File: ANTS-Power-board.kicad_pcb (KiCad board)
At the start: 2 copper layers, 80 x 80 mm, 35 parts, among them J1 DF11-12DP, J2 DF11-12DP, J3 Phoenix 1751248, J4 Phoenix 1751248, U1 TPS62916RPYR, U2 LP2985-3.3

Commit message: Add production files
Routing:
- net VBAT-: vias 140 -> 145
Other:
- board text added: "JLCJLCJLCJLC"

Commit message: Adjust production files
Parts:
- C1, C2: value 22uF -> 10u
- L1: value 1uH -> XGL5030-102MEC

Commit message: Add decoratives
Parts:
- added G***: LOGO, LOGO, F.Cu at (167.5, 108.5)
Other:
- board text added: "+5V/+3.3V LOW-NOISE POWER SUPPLIES"
- board text added: "Designed by Tri Do & Garrett Davis"

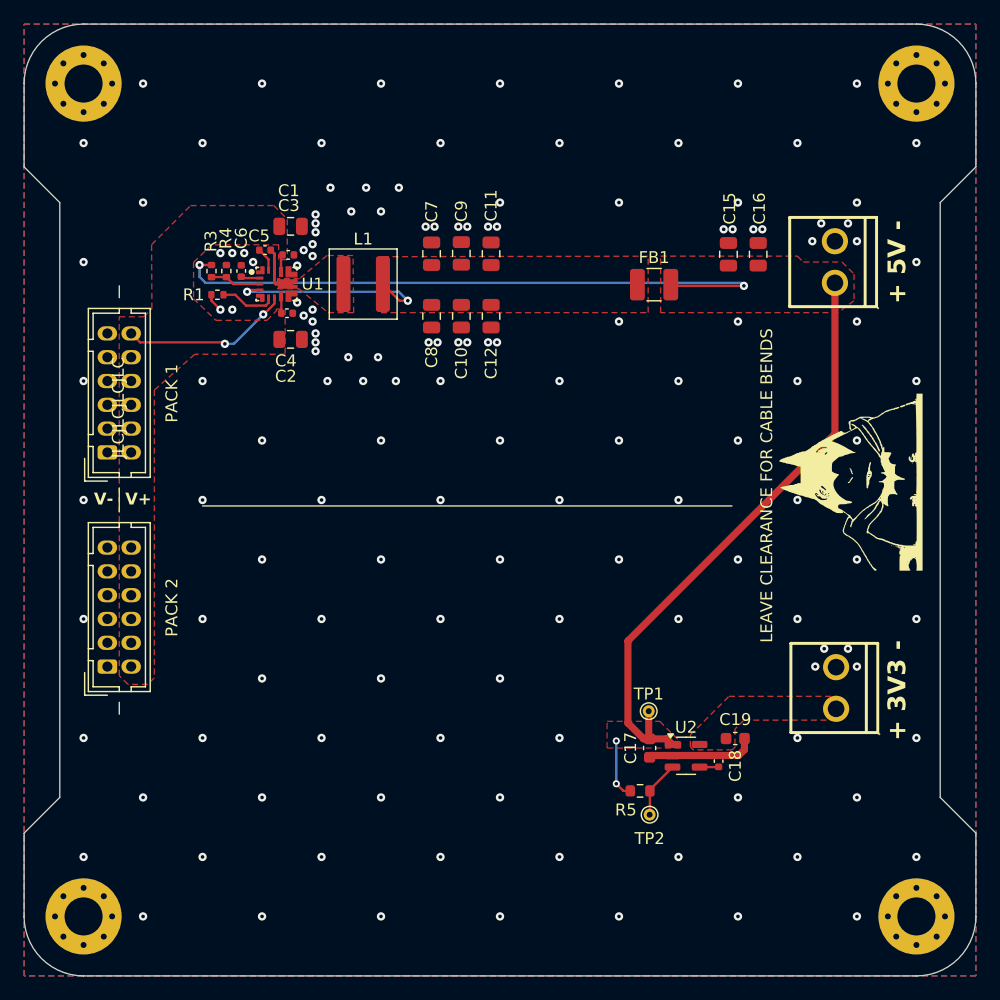
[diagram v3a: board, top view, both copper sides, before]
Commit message: schematic for new DF11 and WJ127 connectors
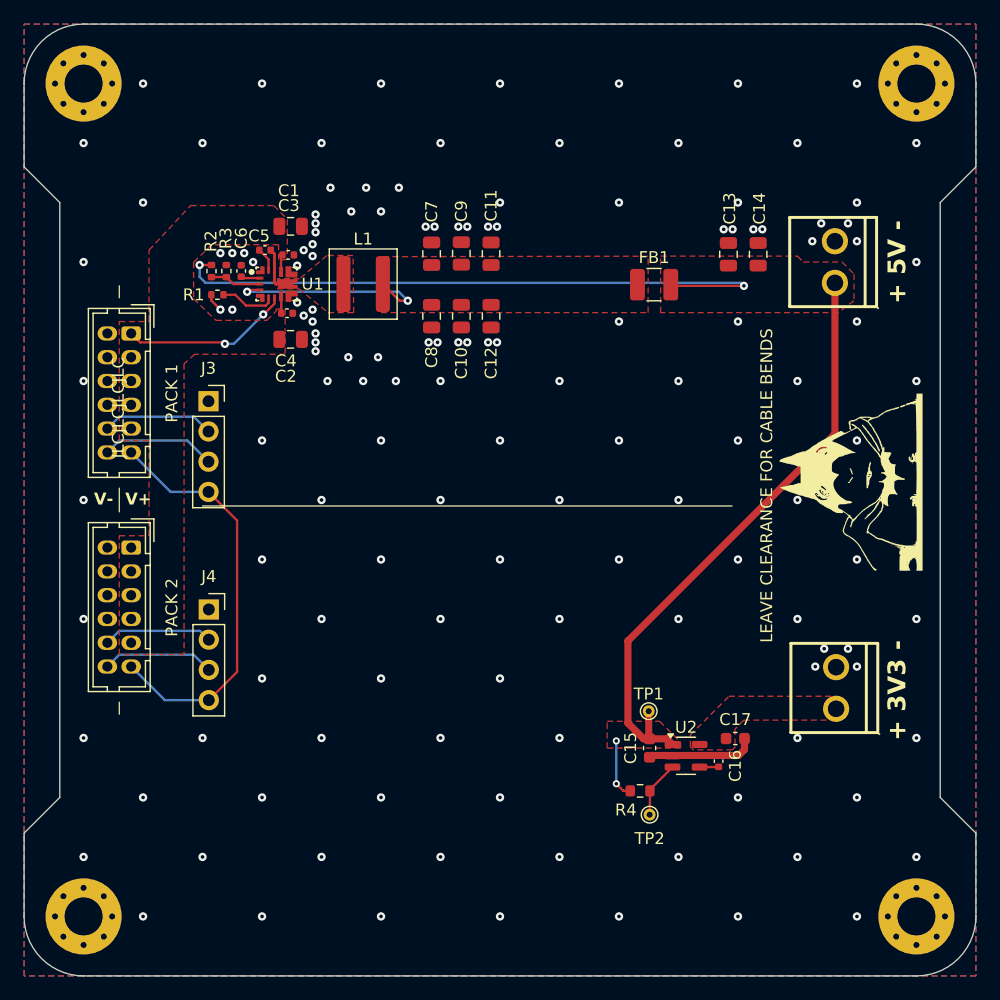
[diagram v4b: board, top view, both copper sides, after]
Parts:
- added J3: Conn_01x04_Pin, Connector_PinSocket_2.54mm:PinSocket_1x04_P2.54mm_Vertical, F.Cu at (115.5, 101.7)
- added J4: Conn_01x04_Pin, Connector_PinSocket_2.54mm:PinSocket_1x04_P2.54mm_Vertical, F.Cu at (115.5, 119.2)
- J5: renamed from J3; value Phoenix 1751248 -> WJ127-5.0-02P-14-00A
- J7: renamed from J4; value Phoenix 1751248 -> WJ127-5.0-02P-14-00A
- moved J1 10.2 mm to (109.0, 96.0), turned to -90 degrees
- moved J2 10.2 mm to (109.0, 114.0), turned to -90 degrees
- renumbered C15 to C13, C16 to C14, C17 to C15, C18 to C16, C19 to C17, R3 to R2, R4 to R3, R5 to R4
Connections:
- J1 pad 1: VBAT- -> VBAT+
- J1 pad 10: VBAT+ -> /SDA_IN1
- J1 pad 11: VBAT- -> +3V3
- J1 pad 12: VBAT+ -> /SCL_IN1
- J1 pad 2: VBAT+ -> VBAT-
- J1 pad 3: VBAT- -> VBAT+
- J1 pad 4: VBAT+ -> VBAT-
- J1 pad 5: VBAT- -> VBAT+
- J1 pad 6: VBAT+ -> VBAT-
- J1 pad 7: VBAT- -> VBAT+
- J1 pad 8: VBAT+ -> VBAT-
- J1 pad 9: VBAT- -> VBAT+
- J2 pad 1: VBAT- -> VBAT+
- J2 pad 10: VBAT+ -> /SDA_IN2
- J2 pad 11: VBAT- -> +3V3
- J2 pad 12: VBAT+ -> /SCL_IN2
- J2 pad 2: VBAT+ -> VBAT-
- J2 pad 3: VBAT- -> VBAT+
- J2 pad 4: VBAT+ -> VBAT-
- J2 pad 5: VBAT- -> VBAT+
- J2 pad 6: VBAT+ -> VBAT-
- J2 pad 7: VBAT- -> VBAT+
- J2 pad 8: VBAT+ -> VBAT-
- J2 pad 9: VBAT- -> VBAT+
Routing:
- net +3V3: track 0.00 -> 35.0 mm
- net /SCL_IN1: track 0.00 -> 9.65 mm
- net /SCL_IN2: track 0.00 -> 9.47 mm
- net /SDA_IN1: track 0.00 -> 9.43 mm
- net /SDA_IN2: track 0.00 -> 9.25 mm
- net VBAT-: vias 145 -> 142

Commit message: update to batt pack v2 (red). add screw terminal
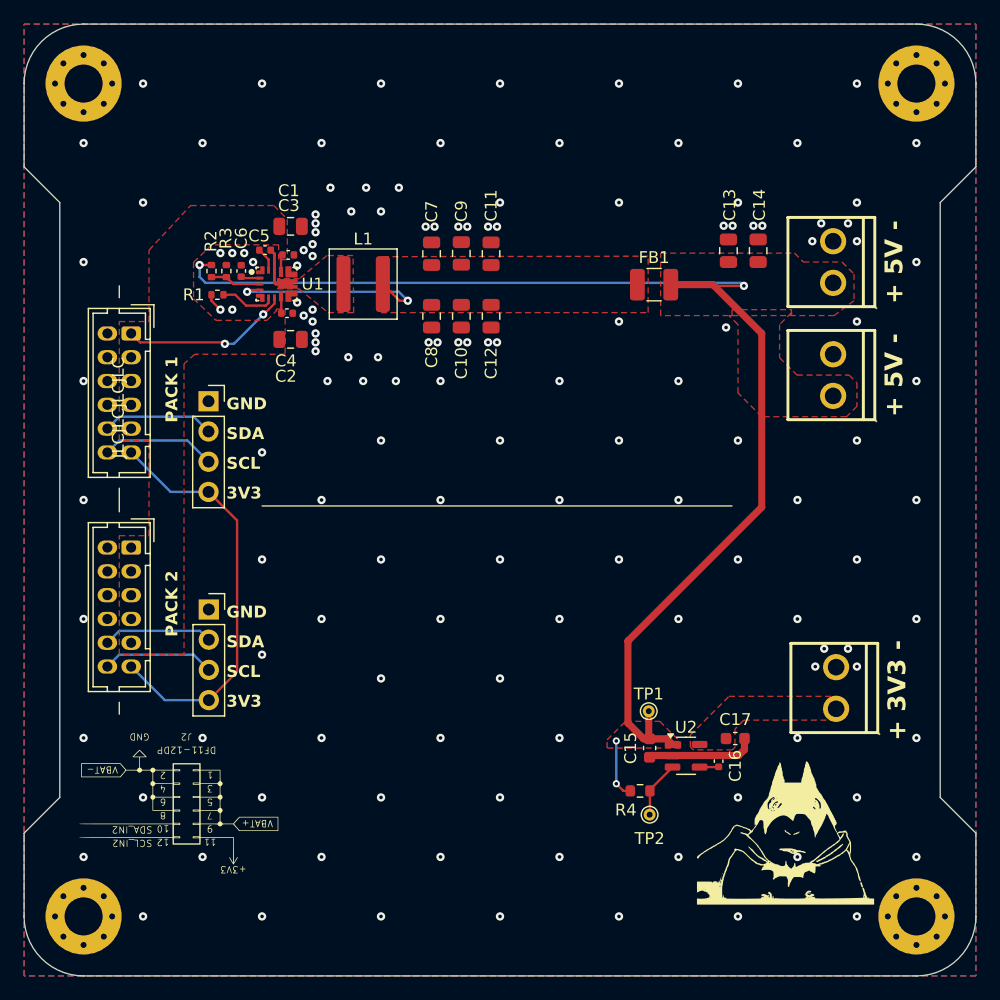
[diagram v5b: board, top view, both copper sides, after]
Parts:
- added G***: LOGO, LOGO, F.Cu at (114.1, 136.2)
- added J6: WJ127-5.0-02P-14-00A, ScrewTerminal:CONN-TH_MKDS1-2-3.5, F.Cu at (168.0, 99.5)
- moved G*** 27.7 mm to (164.0, 136.0), turned to 0 degrees
- moved C13 0.30 mm to (159.2, 89.0)
- moved C14 0.30 mm to (161.7, 89.0)
- moved J5 0.15 mm to (168.0, 90.0)
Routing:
- net 5V_OUTPUT: track 110.3 -> 112.9 mm
- net VBAT-: vias 142 -> 141
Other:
- board text added: "3V3"
- board text added: "GND"
- board text added: "SCL"
- board text added: "SDA"
- board text removed: "LEAVE CLEARANCE FOR CABLE BENDS"
- board text removed: "V+"
- board text removed: "V-"

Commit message: Add decorations
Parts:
- moved G*** 35.5 mm to (134.0, 117.0)
- moved J7 0.25 mm to (168.0, 125.8)
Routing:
- net VBAT-: vias 141 -> 145
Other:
- board text added: "5V @ 6A Low-Noise SMPS. 3V3 @ 150 mA, <30μVrms ripple."
- board text added: "67 yummy"
- board text added: "Do by learning"
- board text added: "Even less noisy than your car"
- board text added: "Have you try turn it off and on again?"
- board text added: "Matcha"
- board text added: "Moose"
- board text added: "Use PROVES BATT Pack v2"
